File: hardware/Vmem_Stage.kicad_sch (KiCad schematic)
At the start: 0 parts

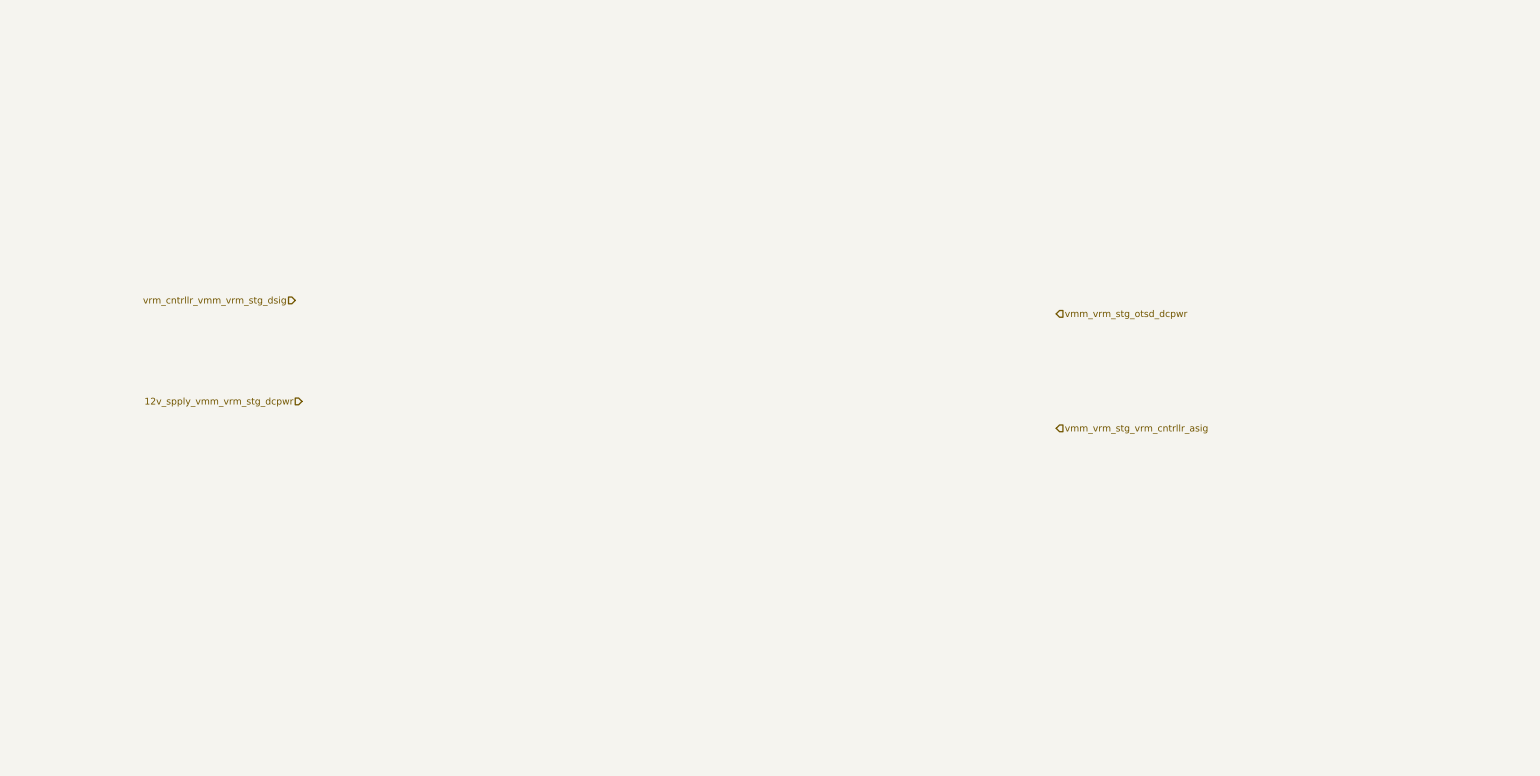
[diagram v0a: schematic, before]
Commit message: feat: Laid-out MOSFET ICs
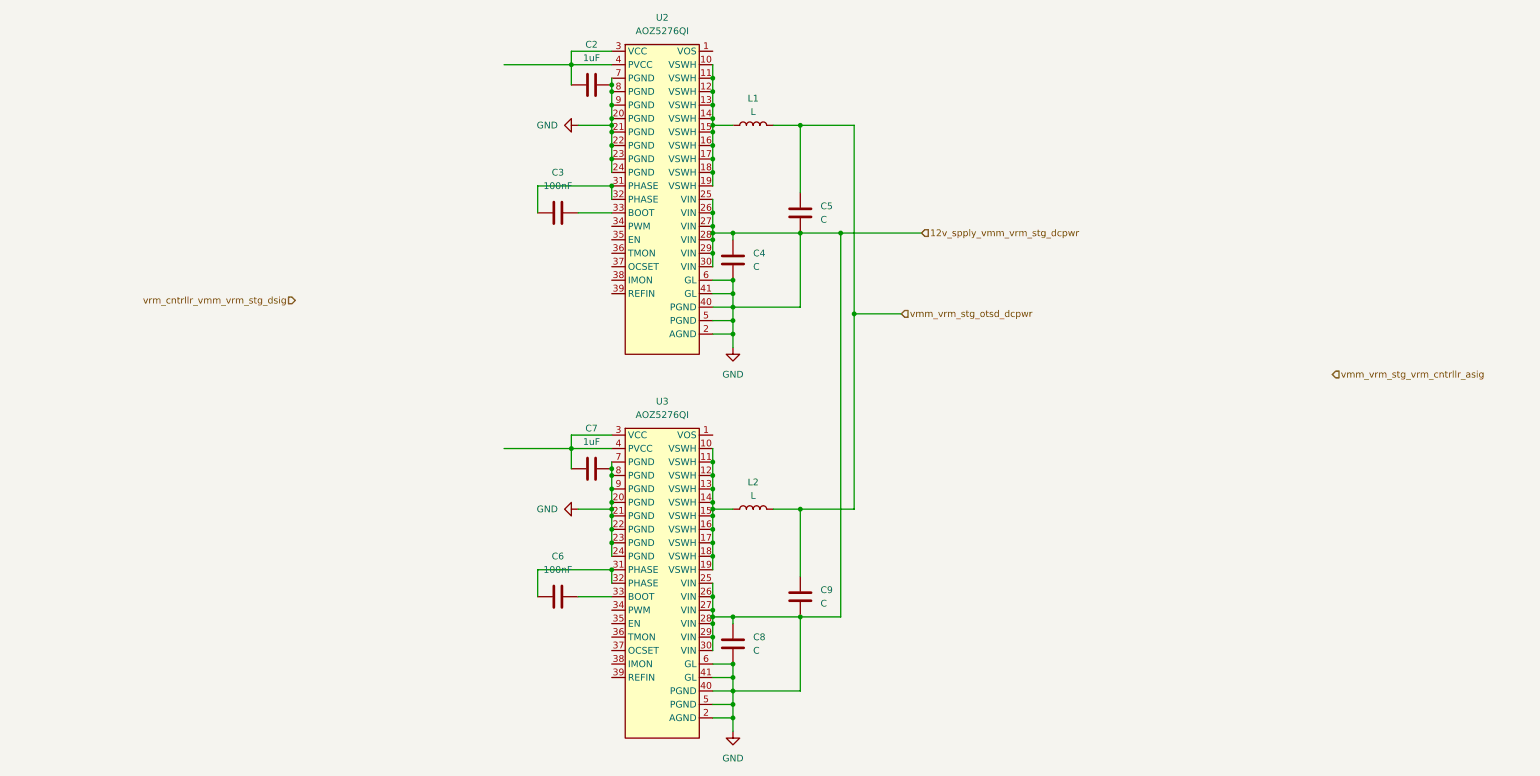
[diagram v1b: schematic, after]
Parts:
- added C2, C7: 1uF, symbol Device:C
- added C3, C6: 100nF, symbol Device:C
- added C4, C5, C8, C9: C, symbol Device:C
- added L1, L2: L, symbol Device:L
- added U2, U3: AOZ5276QI, symbol Symbol_Library:AOZ5276QI
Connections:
- net vmm_vrm_stg_otsd_dcpwr: now also C5.1, C9.1, L1.2, L2.2
- new net: C6.1, U3.31 (PHASE), U3.32 (PHASE)
- new net: C6.2, U3.33 (BOOT)
- new net: L2.1, U3.10 (VSWH), U3.11 (VSWH), U3.12 (VSWH), U3.13 (VSWH), U3.14 (VSWH), U3.15 (VSWH), U3.16 (VSWH), U3.17 (VSWH), U3.18 (VSWH), U3.19 (VSWH)
- new net: C7.1, U3.3 (VCC), U3.4 (PVCC)
- new net: L1.1, U2.10 (VSWH), U2.11 (VSWH), U2.12 (VSWH), U2.13 (VSWH), U2.14 (VSWH), U2.15 (VSWH), U2.16 (VSWH), U2.17 (VSWH), U2.18 (VSWH), U2.19 (VSWH)
- new net: C2.1, U2.3 (VCC), U2.4 (PVCC)
- new net: C3.1, U2.31 (PHASE), U2.32 (PHASE)
- new net: C3.2, U2.33 (BOOT)
- new net GND: C2.2, C4.1, C4.2, C5.2, C7.2, C8.1, C8.2, C9.2, U2.2 (AGND), U2.20 (PGND), U2.21 (PGND), U2.22 (PGND), U2.23 (PGND), U2.24 (PGND), U2.25 (VIN), U2.26 (VIN), U2.27 (VIN), U2.28 (VIN), U2.29 (VIN), U2.30 (VIN), U2.40 (PGND), U2.41 (GL), U2.5 (PGND), U2.6 (GL), U2.7 (PGND), U2.8 (PGND), U2.9 (PGND), U3.2 (AGND), U3.20 (PGND), U3.21 (PGND), U3.22 (PGND), U3.23 (PGND), U3.24 (PGND), U3.25 (VIN), U3.26 (VIN), U3.27 (VIN), U3.28 (VIN), U3.29 (VIN), U3.30 (VIN), U3.40 (PGND), U3.41 (GL), U3.5 (PGND), U3.6 (GL), U3.7 (PGND), U3.8 (PGND), U3.9 (PGND)

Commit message: chore(schematic): Update references
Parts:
- renumbered C3 to C2, C6 to C3, C2 to C4, C7 to C5, C4 to C6, C8 to C7, C5 to C8
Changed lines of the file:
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@@
 		(dnp no)
 		(fields_autoplaced yes)
-		(property "Reference" "C6"
+		(property "Reference" "C3"
 			(at 115.57 118.11 90)
 			(effects
@@
 			(project "gpu-external-power-supply"
 				(path "/d5303413-7068-41ba-88e3-39dfa38d31b7/7e7f036f-1da2-41a9-8561-b6e0c1145c03"
-					(reference "C6")
+					(reference "C3")
 					(unit 1)
 				)
@@
 		(dnp no)
 		(fields_autoplaced yes)
-		(property "Reference" "C2"
+		(property "Reference" "C4"
 			(at 121.92 21.59 90)
 			(effects
@@
 			(project ""
 				(path "/d5303413-7068-41ba-88e3-39dfa38d31b7/7e7f036f-1da2-41a9-8561-b6e0c1145c03"
-					(reference "C2")
+					(reference "C4")
 					(unit 1)
 				)
@@
 		(dnp no)
 		(fields_autoplaced yes)
-		(property "Reference" "#PWR02"
+		(property "Reference" "#PWR04"
 			(at 148.59 85.09 0)
 			(effects
@@
 			(project ""
 				(path "/d5303413-7068-41ba-88e3-39dfa38d31b7/7e7f036f-1da2-41a9-8561-b6e0c1145c03"
-					(reference "#PWR02")
+					(reference "#PWR04")
 					(unit 1)
 				)
@@
 		(dnp no)
 		(fields_autoplaced yes)
-		(property "Reference" "C3"
+		(property "Reference" "C2"
 			(at 115.57 45.72 90)
 			(effects
@@
 			(project ""
 				(path "/d5303413-7068-41ba-88e3-39dfa38d31b7/7e7f036f-1da2-41a9-8561-b6e0c1145c03"
-					(reference "C3")
+					(reference "C2")
 					(unit 1)
 				)
@@
 		(dnp no)
 		(fields_autoplaced yes)
-		(property "Reference" "C7"
+		(property "Reference" "C5"
 			(at 121.92 93.98 90)
 			(effects
@@
 			(project "gpu-external-power-supply"
 				(path "/d5303413-7068-41ba-88e3-39dfa38d31b7/7e7f036f-1da2-41a9-8561-b6e0c1145c03"
-					(reference "C7")
+					(reference "C5")
 					(unit 1)
 				)
@@
 		(dnp no)
 		(fields_autoplaced yes)
-		(property "Reference" "C8"
+		(property "Reference" "C7"
 			(at 152.4 133.3499 0)
 			(effects
@@
 			(project "gpu-external-power-supply"
 				(path "/d5303413-7068-41ba-88e3-39dfa38d31b7/7e7f036f-1da2-41a9-8561-b6e0c1145c03"
-					(reference "C8")
+					(reference "C7")
 					(unit 1)
 				)
@@
 		(dnp no)
 		(fields_autoplaced yes)
-		(property "Reference" "C5"
+		(property "Reference" "C8"
 			(at 165.1 52.0699 0)
 			(effects
@@
 			(project ""
 				(path "/d5303413-7068-41ba-88e3-39dfa38d31b7/7e7f036f-1da2-41a9-8561-b6e0c1145c03"
-					(reference "C5")
+					(reference "C8")
 					(unit 1)
 				)
@@
 		(dnp no)
 		(fields_autoplaced yes)
-		(property "Reference" "#PWR04"
+		(property "Reference" "#PWR03"
 			(at 113.03 109.22 0)
 			(effects
@@
 			(project "gpu-external-power-supply"
 				(path "/d5303413-7068-41ba-88e3-39dfa38d31b7/7e7f036f-1da2-41a9-8561-b6e0c1145c03"
-					(reference "#PWR04")
+					(reference "#PWR03")
 					(unit 1)
 				)
@@
 		(dnp no)
 		(fields_autoplaced yes)
-		(property "Reference" "#PWR03"
+		(property "Reference" "#PWR02"
 			(at 113.03 36.83 0)
 			(effects
@@
 			(project ""
 				(path "/d5303413-7068-41ba-88e3-39dfa38d31b7/7e7f036f-1da2-41a9-8561-b6e0c1145c03"
-					(reference "#PWR03")
+					(reference "#PWR02")
 					(unit 1)
 				)
@@
 		(dnp no)
 		(fields_autoplaced yes)
-		(property "Reference" "C4"
+		(property "Reference" "C6"
 			(at 152.4 60.9599 0)
 			(effects
@@
 			(project ""
 				(path "/d5303413-7068-41ba-88e3-39dfa38d31b7/7e7f036f-1da2-41a9-8561-b6e0c1145c03"
-					(reference "C4")
-					(unit 1)
-				)
+					(reference "C6")
+					(unit 1)
+				)

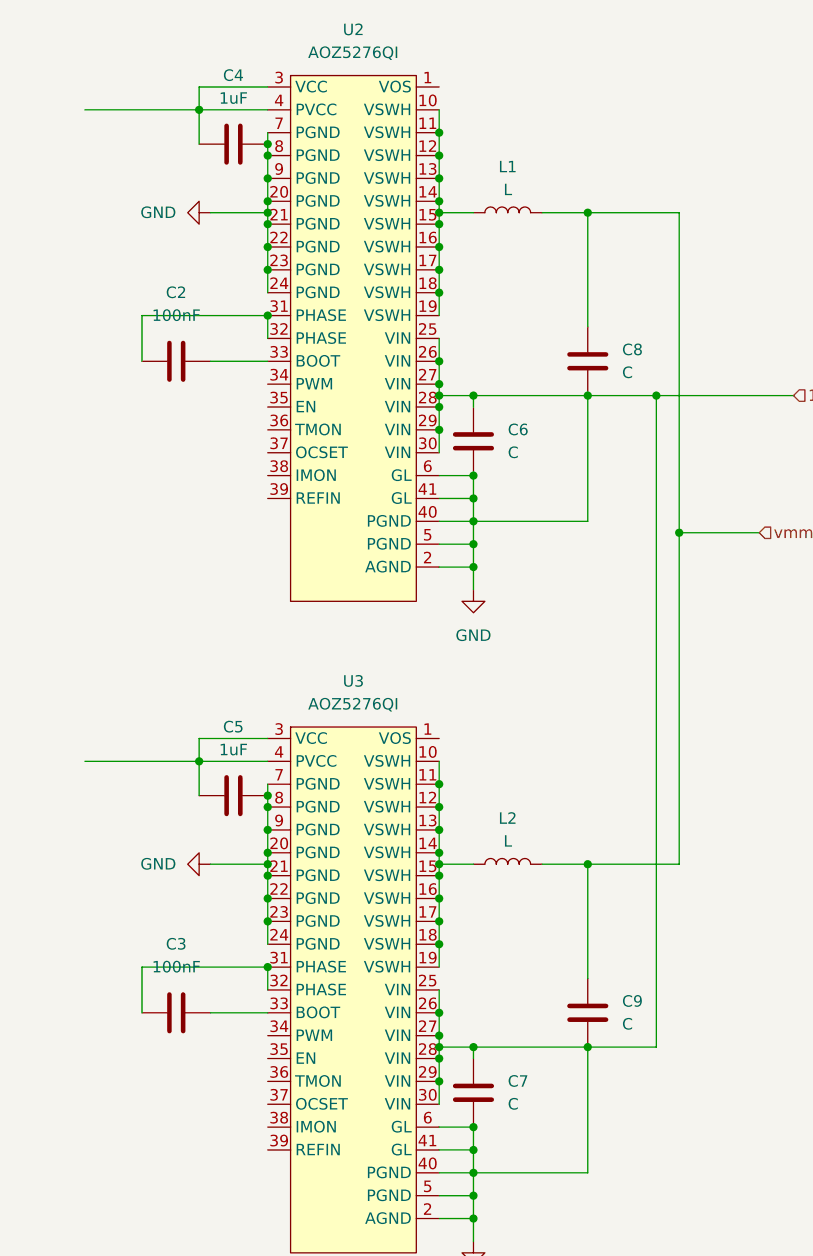
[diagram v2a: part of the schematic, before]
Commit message: Revert "chore(schematic): Update references"
This reverts commit 2cda2d22061e90f93ddb38c43ecf32892cd7b43c.
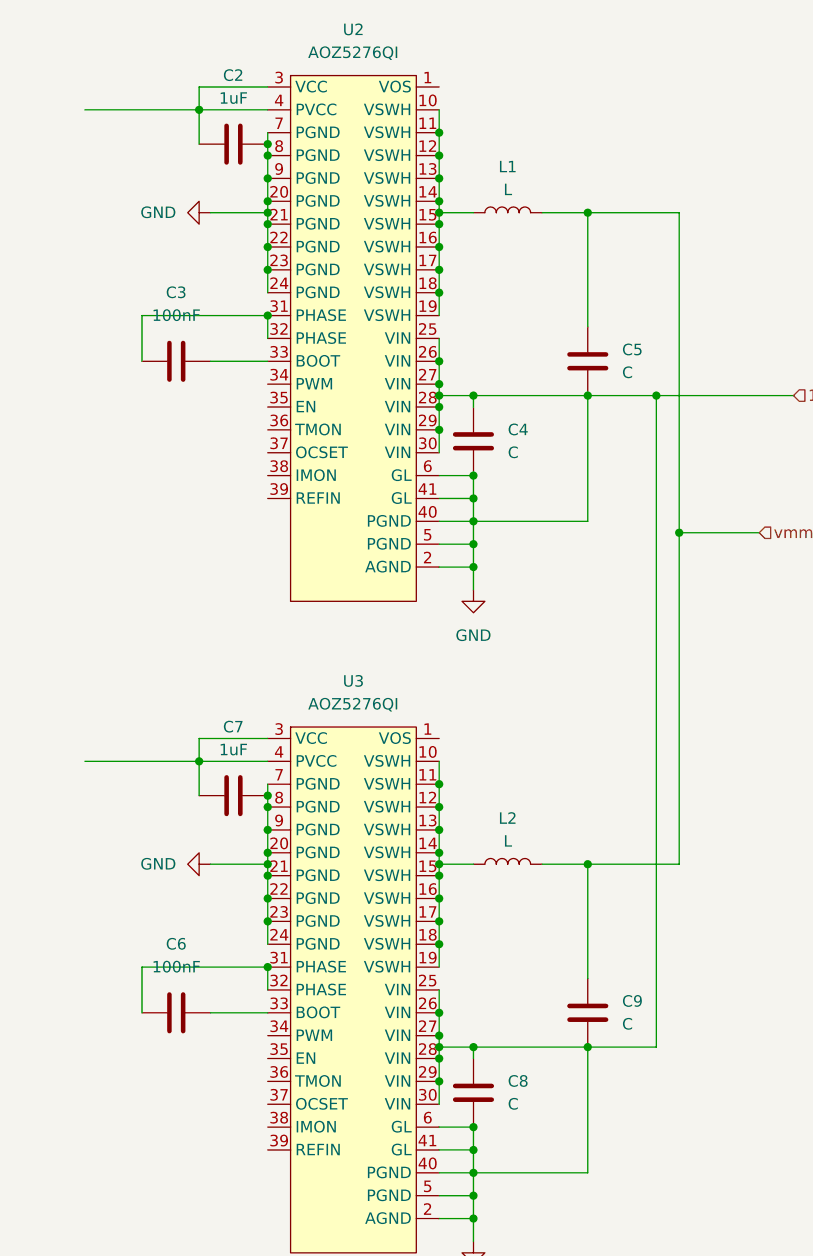
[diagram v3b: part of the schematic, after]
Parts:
- renumbered C4 to C2, C2 to C3, C6 to C4, C8 to C5, C3 to C6, C5 to C7, C7 to C8
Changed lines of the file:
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@@
 		(dnp no)
 		(fields_autoplaced yes)
-		(property "Reference" "C3"
+		(property "Reference" "C6"
 			(at 115.57 118.11 90)
 			(effects
@@
 			(project "gpu-external-power-supply"
 				(path "/d5303413-7068-41ba-88e3-39dfa38d31b7/7e7f036f-1da2-41a9-8561-b6e0c1145c03"
-					(reference "C3")
+					(reference "C6")
 					(unit 1)
 				)
@@
 		(dnp no)
 		(fields_autoplaced yes)
-		(property "Reference" "C4"
+		(property "Reference" "C2"
 			(at 121.92 21.59 90)
 			(effects
@@
 			(project ""
 				(path "/d5303413-7068-41ba-88e3-39dfa38d31b7/7e7f036f-1da2-41a9-8561-b6e0c1145c03"
-					(reference "C4")
+					(reference "C2")
 					(unit 1)
 				)
@@
 		(dnp no)
 		(fields_autoplaced yes)
-		(property "Reference" "#PWR04"
+		(property "Reference" "#PWR02"
 			(at 148.59 85.09 0)
 			(effects
@@
 			(project ""
 				(path "/d5303413-7068-41ba-88e3-39dfa38d31b7/7e7f036f-1da2-41a9-8561-b6e0c1145c03"
-					(reference "#PWR04")
+					(reference "#PWR02")
 					(unit 1)
 				)
@@
 		(dnp no)
 		(fields_autoplaced yes)
-		(property "Reference" "C2"
+		(property "Reference" "C3"
 			(at 115.57 45.72 90)
 			(effects
@@
 			(project ""
 				(path "/d5303413-7068-41ba-88e3-39dfa38d31b7/7e7f036f-1da2-41a9-8561-b6e0c1145c03"
-					(reference "C2")
+					(reference "C3")
 					(unit 1)
 				)
@@
 		(dnp no)
 		(fields_autoplaced yes)
-		(property "Reference" "C5"
+		(property "Reference" "C7"
 			(at 121.92 93.98 90)
 			(effects
@@
 			(project "gpu-external-power-supply"
 				(path "/d5303413-7068-41ba-88e3-39dfa38d31b7/7e7f036f-1da2-41a9-8561-b6e0c1145c03"
-					(reference "C5")
+					(reference "C7")
 					(unit 1)
 				)
@@
 		(dnp no)
 		(fields_autoplaced yes)
-		(property "Reference" "C7"
+		(property "Reference" "C8"
 			(at 152.4 133.3499 0)
 			(effects
@@
 			(project "gpu-external-power-supply"
 				(path "/d5303413-7068-41ba-88e3-39dfa38d31b7/7e7f036f-1da2-41a9-8561-b6e0c1145c03"
-					(reference "C7")
+					(reference "C8")
 					(unit 1)
 				)
@@
 		(dnp no)
 		(fields_autoplaced yes)
-		(property "Reference" "C8"
+		(property "Reference" "C5"
 			(at 165.1 52.0699 0)
 			(effects
@@
 			(project ""
 				(path "/d5303413-7068-41ba-88e3-39dfa38d31b7/7e7f036f-1da2-41a9-8561-b6e0c1145c03"
-					(reference "C8")
+					(reference "C5")
 					(unit 1)
 				)
@@
 		(dnp no)
 		(fields_autoplaced yes)
-		(property "Reference" "#PWR03"
+		(property "Reference" "#PWR04"
 			(at 113.03 109.22 0)
 			(effects
@@
 			(project "gpu-external-power-supply"
 				(path "/d5303413-7068-41ba-88e3-39dfa38d31b7/7e7f036f-1da2-41a9-8561-b6e0c1145c03"
-					(reference "#PWR03")
+					(reference "#PWR04")
 					(unit 1)
 				)
@@
 		(dnp no)
 		(fields_autoplaced yes)
-		(property "Reference" "#PWR02"
+		(property "Reference" "#PWR03"
 			(at 113.03 36.83 0)
 			(effects
@@
 			(project ""
 				(path "/d5303413-7068-41ba-88e3-39dfa38d31b7/7e7f036f-1da2-41a9-8561-b6e0c1145c03"
-					(reference "#PWR02")
+					(reference "#PWR03")
 					(unit 1)
 				)
@@
 		(dnp no)
 		(fields_autoplaced yes)
-		(property "Reference" "C6"
+		(property "Reference" "C4"
 			(at 152.4 60.9599 0)
 			(effects
@@
 			(project ""
 				(path "/d5303413-7068-41ba-88e3-39dfa38d31b7/7e7f036f-1da2-41a9-8561-b6e0c1145c03"
-					(reference "C6")
-					(unit 1)
-				)
+					(reference "C4")
+					(unit 1)
+				)

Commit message: chore: update project references
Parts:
- renumbered C3 to C3001, C6 to C3002, C2 to C3003, C7 to C3004, C4 to C3005, C8 to C3006, C5 to C3007, C9 to C3008, L1 to L3001, L2 to L3002, U2 to U3001, U3 to U3002
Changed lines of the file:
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@@
 		(dnp no)
 		(fields_autoplaced yes)
-		(property "Reference" "C6"
+		(property "Reference" "C3002"
 			(at 115.57 118.11 90)
 			(effects
@@
 			(project "gpu-external-power-supply"
 				(path "/d5303413-7068-41ba-88e3-39dfa38d31b7/7e7f036f-1da2-41a9-8561-b6e0c1145c03"
-					(reference "C6")
+					(reference "C3002")
 					(unit 1)
 				)
@@
 		(dnp no)
 		(fields_autoplaced yes)
-		(property "Reference" "U3"
+		(property "Reference" "U3002"
 			(at 135.255 88.9 0)
 			(effects
@@
 			(project "gpu-external-power-supply"
 				(path "/d5303413-7068-41ba-88e3-39dfa38d31b7/7e7f036f-1da2-41a9-8561-b6e0c1145c03"
-					(reference "U3")
+					(reference "U3002")
 					(unit 1)
 				)
@@
 		(dnp no)
 		(fields_autoplaced yes)
-		(property "Reference" "L2"
+		(property "Reference" "L3002"
 			(at 152.4 104.14 90)
 			(effects
@@
 			(project "gpu-external-power-supply"
 				(path "/d5303413-7068-41ba-88e3-39dfa38d31b7/7e7f036f-1da2-41a9-8561-b6e0c1145c03"
-					(reference "L2")
+					(reference "L3002")
 					(unit 1)
 				)
@@
 		(dnp no)
 		(fields_autoplaced yes)
-		(property "Reference" "U2"
+		(property "Reference" "U3001"
 			(at 135.255 16.51 0)
 			(effects
@@
 			(project ""
 				(path "/d5303413-7068-41ba-88e3-39dfa38d31b7/7e7f036f-1da2-41a9-8561-b6e0c1145c03"
-					(reference "U2")
+					(reference "U3001")
 					(unit 1)
 				)
@@
 		(dnp no)
 		(fields_autoplaced yes)
-		(property "Reference" "C2"
+		(property "Reference" "C3003"
 			(at 121.92 21.59 90)
 			(effects
@@
 			(project ""
 				(path "/d5303413-7068-41ba-88e3-39dfa38d31b7/7e7f036f-1da2-41a9-8561-b6e0c1145c03"
-					(reference "C2")
+					(reference "C3003")
 					(unit 1)
 				)
@@
 		(dnp no)
 		(fields_autoplaced yes)
-		(property "Reference" "L1"
+		(property "Reference" "L3001"
 			(at 152.4 31.75 90)
 			(effects
@@
 			(project ""
 				(path "/d5303413-7068-41ba-88e3-39dfa38d31b7/7e7f036f-1da2-41a9-8561-b6e0c1145c03"
-					(reference "L1")
+					(reference "L3001")
 					(unit 1)
 				)
@@
 		(dnp no)
 		(fields_autoplaced yes)
-		(property "Reference" "#PWR05"
+		(property "Reference" "#PWR03004"
 			(at 148.59 157.48 0)
 			(effects
@@
 			(project "gpu-external-power-supply"
 				(path "/d5303413-7068-41ba-88e3-39dfa38d31b7/7e7f036f-1da2-41a9-8561-b6e0c1145c03"
-					(reference "#PWR05")
+					(reference "#PWR03004")
 					(unit 1)
 				)
@@
 		(dnp no)
 		(fields_autoplaced yes)
-		(property "Reference" "#PWR02"
+		(property "Reference" "#PWR03003"
 			(at 148.59 85.09 0)
 			(effects
@@
 			(project ""
 				(path "/d5303413-7068-41ba-88e3-39dfa38d31b7/7e7f036f-1da2-41a9-8561-b6e0c1145c03"
-					(reference "#PWR02")
+					(reference "#PWR03003")
 					(unit 1)
 				)
@@
 		(dnp no)
 		(fields_autoplaced yes)
-		(property "Reference" "C3"
+		(property "Reference" "C3001"
 			(at 115.57 45.72 90)
 			(effects
@@
 			(project ""
 				(path "/d5303413-7068-41ba-88e3-39dfa38d31b7/7e7f036f-1da2-41a9-8561-b6e0c1145c03"
-					(reference "C3")
+					(reference "C3001")
 					(unit 1)
 				)
@@
 		(dnp no)
 		(fields_autoplaced yes)
-		(property "Reference" "C7"
+		(property "Reference" "C3004"
 			(at 121.92 93.98 90)
 			(effects
@@
 			(project "gpu-external-power-supply"
 				(path "/d5303413-7068-41ba-88e3-39dfa38d31b7/7e7f036f-1da2-41a9-8561-b6e0c1145c03"
-					(reference "C7")
+					(reference "C3004")
 					(unit 1)
 				)
@@
 		(dnp no)
 		(fields_autoplaced yes)
-		(property "Reference" "C9"
+		(property "Reference" "C3008"
 			(at 165.1 124.4599 0)
 			(effects
@@
 			(project "gpu-external-power-supply"
 				(path "/d5303413-7068-41ba-88e3-39dfa38d31b7/7e7f036f-1da2-41a9-8561-b6e0c1145c03"
-					(reference "C9")
+					(reference "C3008")
 					(unit 1)
 				)
@@
 		(dnp no)
 		(fields_autoplaced yes)
-		(property "Reference" "C8"
+		(property "Reference" "C3006"
 			(at 152.4 133.3499 0)
 			(effects
@@
 			(project "gpu-external-power-supply"
 				(path "/d5303413-7068-41ba-88e3-39dfa38d31b7/7e7f036f-1da2-41a9-8561-b6e0c1145c03"
-					(reference "C8")
+					(reference "C3006")
 					(unit 1)
 				)
@@
 		(dnp no)
 		(fields_autoplaced yes)
-		(property "Reference" "C5"
+		(property "Reference" "C3007"
 			(at 165.1 52.0699 0)
 			(effects
@@
 			(project ""
 				(path "/d5303413-7068-41ba-88e3-39dfa38d31b7/7e7f036f-1da2-41a9-8561-b6e0c1145c03"
-					(reference "C5")
+					(reference "C3007")
 					(unit 1)
 				)
@@
 		(dnp no)
 		(fields_autoplaced yes)
-		(property "Reference" "#PWR04"
+		(property "Reference" "#PWR03002"
 			(at 113.03 109.22 0)
 			(effects
@@
 			(project "gpu-external-power-supply"
 				(path "/d5303413-7068-41ba-88e3-39dfa38d31b7/7e7f036f-1da2-41a9-8561-b6e0c1145c03"
-					(reference "#PWR04")
+					(reference "#PWR03002")
 					(unit 1)
 				)
@@
 		(dnp no)
 		(fields_autoplaced yes)
-		(property "Reference" "#PWR03"
+		(property "Reference" "#PWR03001"
 			(at 113.03 36.83 0)
 			(effects
@@
 			(project ""
 				(path "/d5303413-7068-41ba-88e3-39dfa38d31b7/7e7f036f-1da2-41a9-8561-b6e0c1145c03"
-					(reference "#PWR03")
+					(reference "#PWR03001")
 					(unit 1)
 				)
@@
 		(dnp no)
 		(fields_autoplaced yes)
-		(property "Reference" "C4"
+		(property "Reference" "C3005"
 			(at 152.4 60.9599 0)
 			(effects
@@
 			(project ""
 				(path "/d5303413-7068-41ba-88e3-39dfa38d31b7/7e7f036f-1da2-41a9-8561-b6e0c1145c03"
-					(reference "C4")
-					(unit 1)
-				)
+					(reference "C3005")
+					(unit 1)
+				)
